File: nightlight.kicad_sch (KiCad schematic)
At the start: 44 parts, among them J1 Conn_01x06_Pin, SW1 SKRTLAE010, SW2 SKRTLAE010, SW3 SW_Push, SW4 SW_Push, U1 ESP-12F, U2 USB-TYPE-C-009, U4 AMS1117-3.3

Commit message: Rearrange front side Add images, readme
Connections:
- net GND: now also SW3.2; no longer SW3.1
- net RX: now also J1.6 (Pin_6); no longer J1.3 (Pin_3)
- net TX: now also J1.5 (Pin_5); no longer J1.4 (Pin_4)
- net program: now also J1.4 (Pin_4); no longer J1.5 (Pin_5)
- net reset: now also J1.3 (Pin_3), SW3.1; no longer J1.6 (Pin_6), SW3.2
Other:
- moved on the sheet: SW3
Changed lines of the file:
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@@
+    (stroke (width 0) (type default))
+  )
+  (wire (pts (xy 107.95 81.28) (xy 115.57 81.28))
     (stroke (width 0) (type default))
   )
@@
     (stroke (width 0) (type default))
   )
+  (wire (pts (xy 107.95 83.82) (xy 115.57 83.82))
+    (stroke (width 0) (type default))
+  )
   (wire (pts (xy 184.15 124.46) (xy 209.55 124.46))
     (stroke (width 0) (type default))
@@
     (stroke (width 0) (type default))
   )
-  (wire (pts (xy 107.95 83.82) (xy 115.57 83.82))
-    (stroke (width 0) (type default))
-  )
   (wire (pts (xy 63.5 77.47) (xy 63.5 80.01))
     (stroke (width 0) (type default))
@@
     (stroke (width 0) (type default))
   )
+  (wire (pts (xy 107.95 86.36) (xy 115.57 86.36))
+    (stroke (width 0) (type default))
+  )
+  (wire (pts (xy 107.95 78.74) (xy 115.57 78.74))
+    (stroke (width 0) (type default))
+  )
   (wire (pts (xy 234.95 66.04) (xy 260.35 66.04))
     (stroke (width 0) (type default))
@@
     (stroke (width 0) (type default))
   )
-  (wire (pts (xy 107.95 81.28) (xy 115.57 81.28))
-    (stroke (width 0) (type default))
-  )
   (wire (pts (xy 184.15 74.93) (xy 184.15 73.66))
     (stroke (width 0) (type default))
@@
     (stroke (width 0) (type default))
   )
-  (wire (pts (xy 107.95 86.36) (xy 115.57 86.36))
-    (stroke (width 0) (type default))
-  )
   (wire (pts (xy 41.91 109.22) (xy 41.91 121.92))
     (stroke (width 0) (type default))
@@
     (stroke (width 0) (type default))
   )
-  (wire (pts (xy 107.95 78.74) (xy 115.57 78.74))
-    (stroke (width 0) (type default))
-  )
   (wire (pts (xy 100.33 137.16) (xy 106.68 137.16))
     (stroke (width 0) (type default))
@@
     (effects (font (size 1.27 1.27)) (justify left bottom))
   )
-  (label "RX" (at 115.57 78.74 0) (fields_autoplaced)
+  (label "RX" (at 115.57 86.36 0) (fields_autoplaced)
     (effects (font (size 1.27 1.27)) (justify left bottom))
   )
@@
     (effects (font (size 1.27 1.27)) (justify left bottom))
   )
-  (label "TX" (at 115.57 81.28 0) (fields_autoplaced)
+  (label "TX" (at 115.57 83.82 0) (fields_autoplaced)
     (effects (font (size 1.27 1.27)) (justify left bottom))
   )
@@
     (effects (font (size 1.27 1.27)) (justify left bottom))
   )
-  (label "program" (at 115.57 83.82 0) (fields_autoplaced)
-    (effects (font (size 1.27 1.27)) (justify left bottom))
-  )
-  (label "reset" (at 115.57 86.36 0) (fields_autoplaced)
+  (label "program" (at 115.57 81.28 0) (fields_autoplaced)
+    (effects (font (size 1.27 1.27)) (justify left bottom))
+  )
+  (label "reset" (at 115.57 78.74 0) (fields_autoplaced)
     (effects (font (size 1.27 1.27)) (justify left bottom))
   )
@@
     )
   )
-  (symbol (lib_id "Switch:SW_Push") (at 22.86 44.45 0) (unit 1)
-    (in_bom yes) (on_board yes) (dnp no) (fields_autoplaced)
-    (property "Reference" "SW3" (at 22.86 36.83 0)
-      (effects (font (size 1.27 1.27)))
-    )
-    (property "Value" "SW_Push" (at 22.86 39.37 0)
-      (effects (font (size 1.27 1.27)))
-    )
-    (property "Footprint" "nightlight:SW-SMD_L3.9-W3.0-P4.45" (at 22.86 39.37 0)
-      (effects (font (size 1.27 1.27)) hide)
-    )
-    (property "Datasheet" "~" (at 22.86 39.37 0)
-      (effects (font (size 1.27 1.27)) hide)
-    )
+  (symbol (lib_id "Switch:SW_Push") (at 22.86 44.45 180) (unit 1)
+    (in_bom yes) (on_board yes) (dnp no) (fields_autoplaced)
+    (property "Reference" "SW3" (at 22.86 39.37 0)
+      (effects (font (size 1.27 1.27)))
+    )
+    (property "Value" "SW_Push" (at 22.86 41.91 0)
+      (effects (font (size 1.27 1.27)))
+    )
+    (property "Footprint" "nightlight:SW-SMD_L3.9-W3.0-P4.45" (at 22.86 49.53 0)
+      (effects (font (size 1.27 1.27)) hide)
+    )
+    (property "Datasheet" "~" (at 22.86 49.53 0)
+      (effects (font (size 1.27 1.27)) hide)
+    )

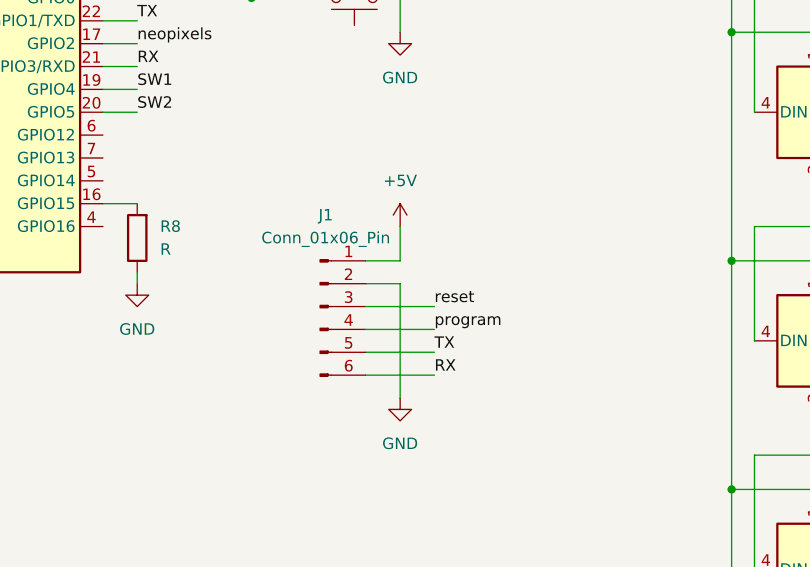
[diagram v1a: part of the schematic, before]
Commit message: flip gnd and 5v on flash pins
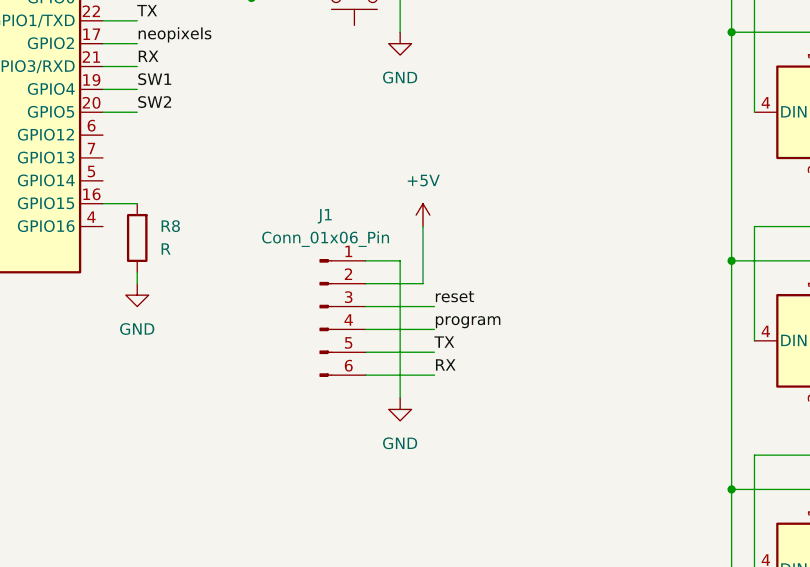
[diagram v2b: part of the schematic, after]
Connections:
- net +5V: now also J1.2 (Pin_2); no longer J1.1 (Pin_1)
- net GND: now also J1.1 (Pin_1); no longer J1.2 (Pin_2)

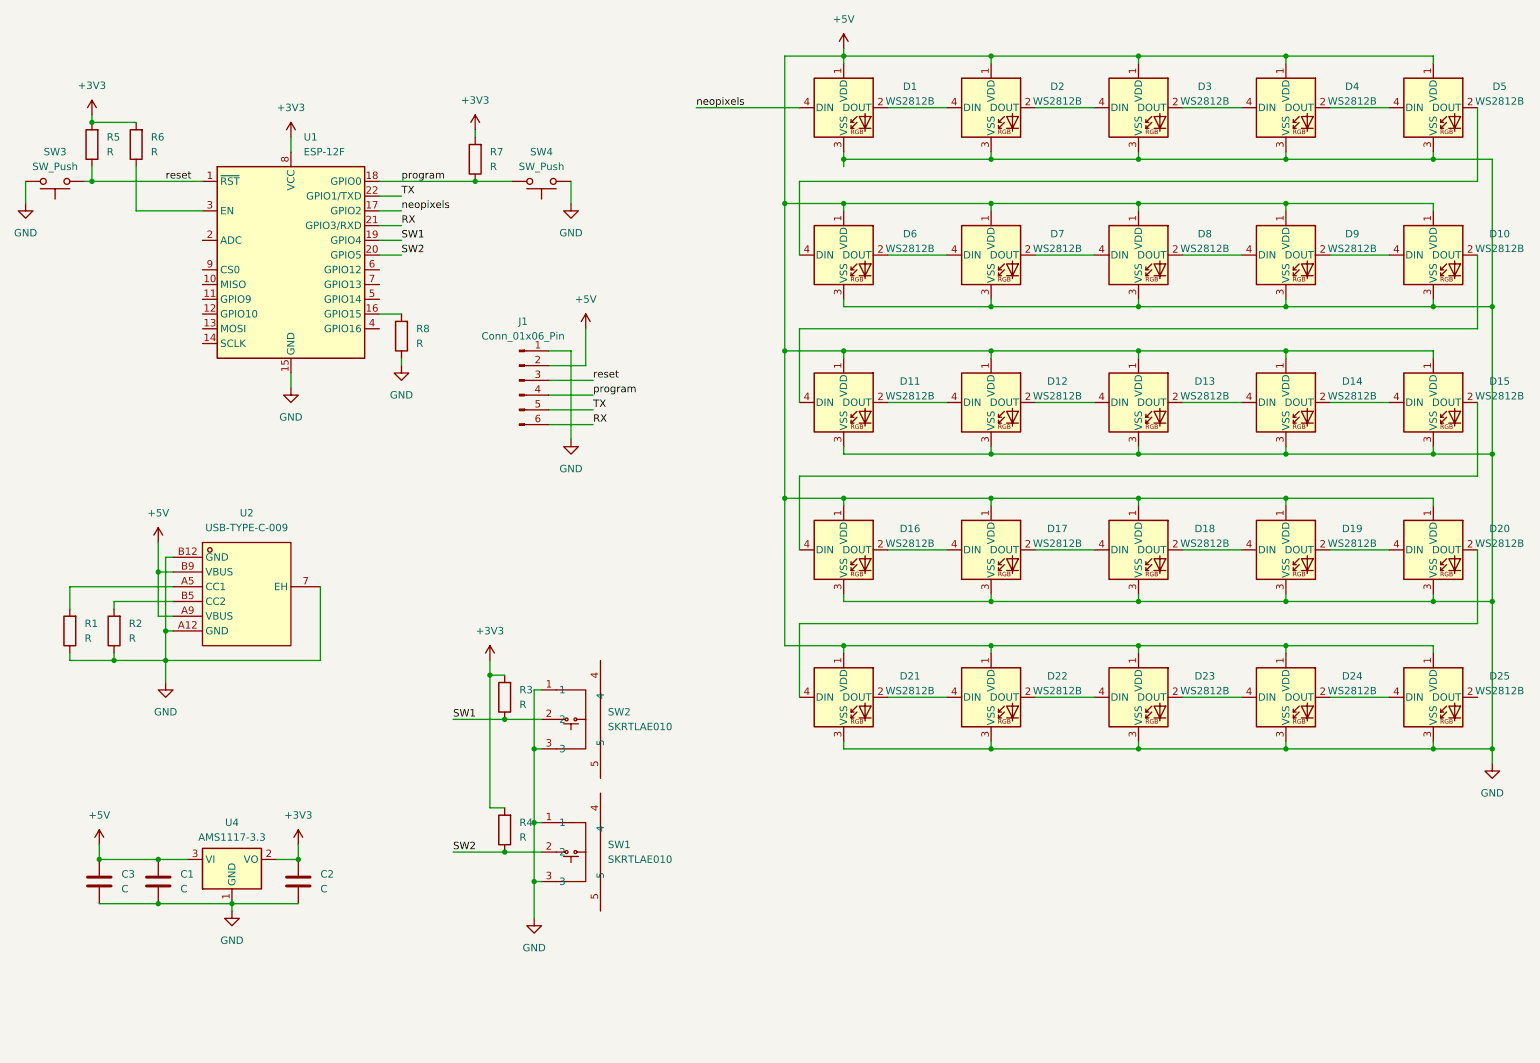
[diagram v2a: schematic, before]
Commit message: Add C4, C5 Remove J1 Add pads for flashing Add level shifter
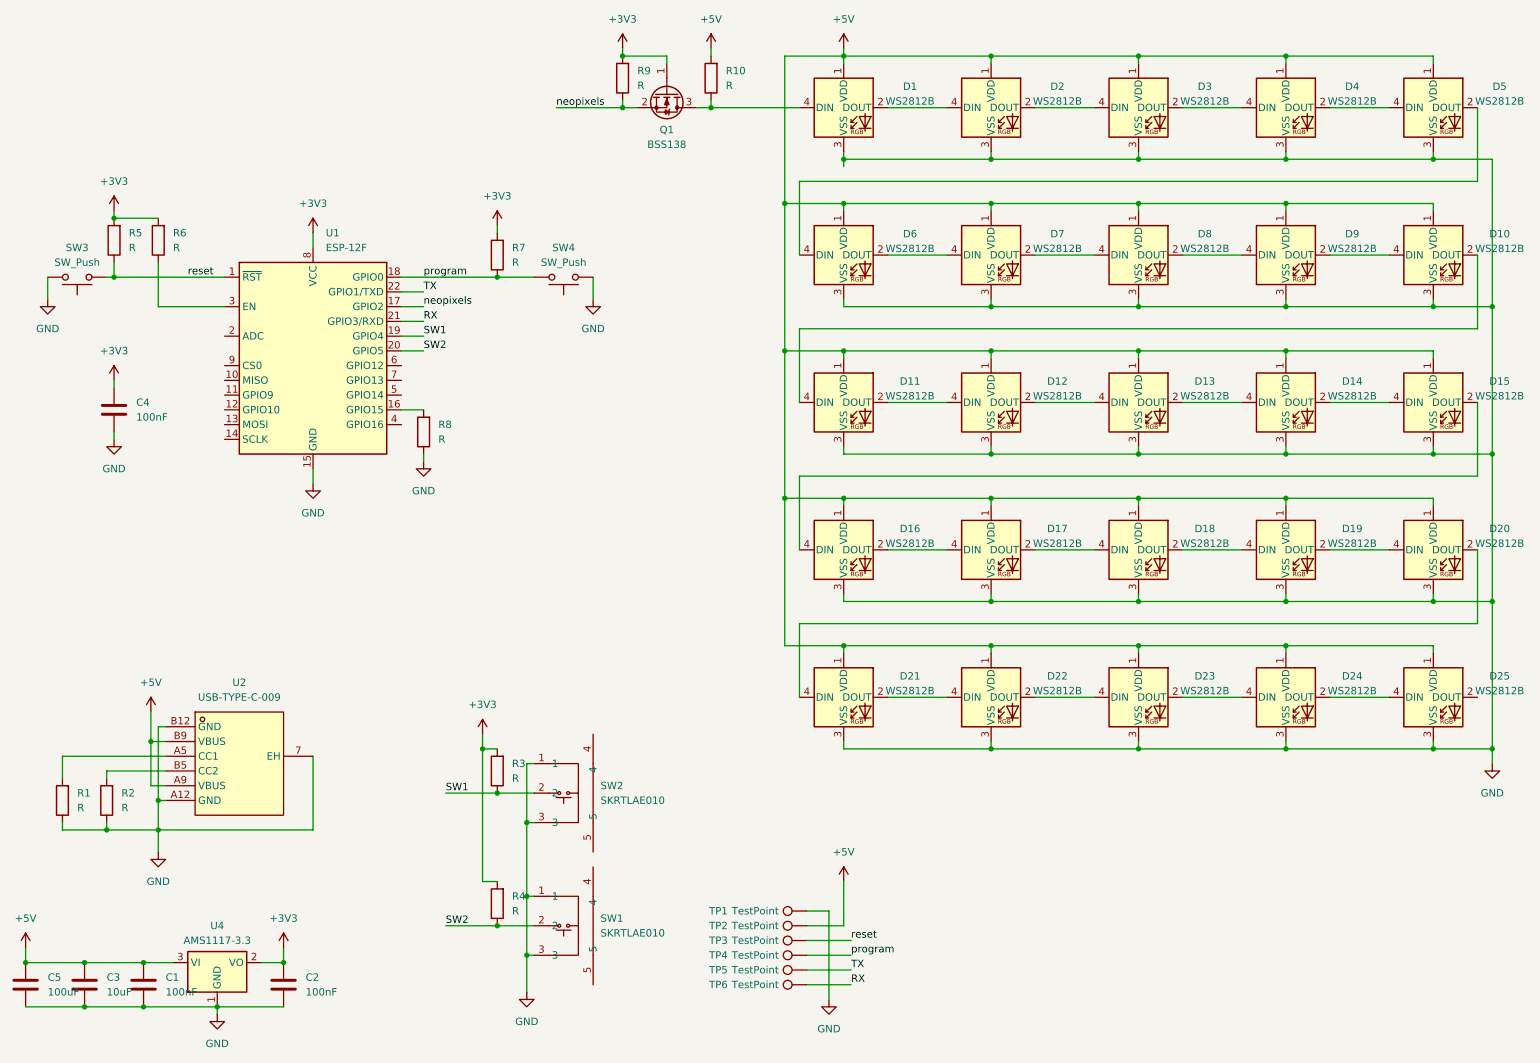
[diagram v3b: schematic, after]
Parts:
- removed J1: Conn_01x06_Pin, Connector_PinHeader_2.54mm:PinHeader_1x06_P2.54mm_Horizontal, symbol Connector:Conn_01x06_Pin
- added C4: 100nF, Capacitor_SMD:C_0402_1005Metric, symbol Device:C
- added C5: 100uF, Capacitor_SMD:C_1210_3225Metric, symbol Device:C
- added Q1: BSS138, Package_TO_SOT_SMD:SOT-23, symbol Transistor_FET:BSS138
- added R10, R9: R, Resistor_SMD:R_0603_1608Metric, symbol Device:R
- added TP1, TP2, TP3, TP4, TP5, TP6: TestPoint, TestPoint:TestPoint_Pad_D1.5mm, symbol Connector:TestPoint
- C1, C2: value C -> 100nF
- C3: value C -> 10uF
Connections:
- net +3V3: now also C4.1, Q1.1 (G), R9.2
- net +5V: now also C5.1, R10.2, TP2.1
- net GND: now also C4.2, C5.2, TP1.1
- net RX: now also TP6.1
- net TX: now also TP5.1
- net neopixels: now also Q1.2 (S), R9.1; no longer D1.4 (DIN)
- net program: now also TP4.1
- net reset: now also TP3.1
- new net: D1.4 (DIN), Q1.3 (D), R10.1
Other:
- moved on the sheet: C1, C2, C3, R1, R2, R3, R4, R5, R6, R7, R8, SW1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
